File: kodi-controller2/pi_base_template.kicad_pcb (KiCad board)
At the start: 2 copper layers, 62 x 62.9 mm, 17 parts, among them P1 Raspberry_Pi_+_Conn, SW1 SW_PUSH_SMALL, SW2 SW_PUSH_SMALL, SW3 SW_PUSH_SMALL, SW4 SW_PUSH_SMALL

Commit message: Finished new board layout
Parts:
- moved R2 2.54 mm to (145.1, 114.4)
- turned P1 to 180 degrees
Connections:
- P1 pad 10: (no net) -> Net-(P1-Pad19)
- P1 pad 11: Net-(P1-Pad11) -> Net-(P1-Pad21)
- P1 pad 12: (no net) -> Net-(P1-Pad23)
- P1 pad 13: Net-(P1-Pad13) -> GND
- P1 pad 15: Net-(P1-Pad15) -> Net-(P1-Pad29)
- P1 pad 16: (no net) -> Net-(P1-Pad31)
- P1 pad 19: Net-(P1-Pad19) -> (no net)
- P1 pad 2: (no net) -> Net-(P1-Pad3)
- P1 pad 20: (no net) -> GND
- P1 pad 3: Net-(P1-Pad3) -> (no net)
- P1 pad 4: (no net) -> Net-(P1-Pad7)
- P1 pad 5: Net-(P1-Pad5) -> GND
- P1 pad 6: (no net) -> Net-(P1-Pad11)
- P1 pad 7: Net-(P1-Pad7) -> Net-(P1-Pad13)
- P1 pad 8: (no net) -> Net-(P1-Pad15)
- P1 pad 9: GND -> +3V3
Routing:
- net GND: track 0.00 -> 143.2 mm
- net +3V3: track 0.00 -> 127.2 mm, vias 0 -> 5
- net Net-(P1-Pad11): track 0.00 -> 73.4 mm
- net Net-(P1-Pad3): track 0.00 -> 69.1 mm
- net Net-(P1-Pad7): track 0.00 -> 68.5 mm
- net Net-(P1-Pad13): track 0.00 -> 58.6 mm
- net Net-(P1-Pad15): track 0.00 -> 45.2 mm
- net Net-(P1-Pad19): track 0.00 -> 43.1 mm
- net Net-(P1-Pad21): track 0.00 -> 33.6 mm
- net Net-(P1-Pad31): track 0.00 -> 29.0 mm
- net Net-(P1-Pad23): track 0.00 -> 27.3 mm
- net Net-(P1-Pad29): track 0.00 -> 25.2 mm
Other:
- board size 62 x 62.9 mm -> 109.2 x 62.9 mm

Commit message: KodeController2: Switched footprint pin positions for push switches.
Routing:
- net GND: track 143.2 -> 147.3 mm
- net Net-(P1-Pad19): track 43.1 -> 41.4 mm
- net Net-(P1-Pad15): track 45.2 -> 46.5 mm
- net Net-(P1-Pad13): track 58.6 -> 59.9 mm
- net Net-(P1-Pad21): track 33.6 -> 34.9 mm

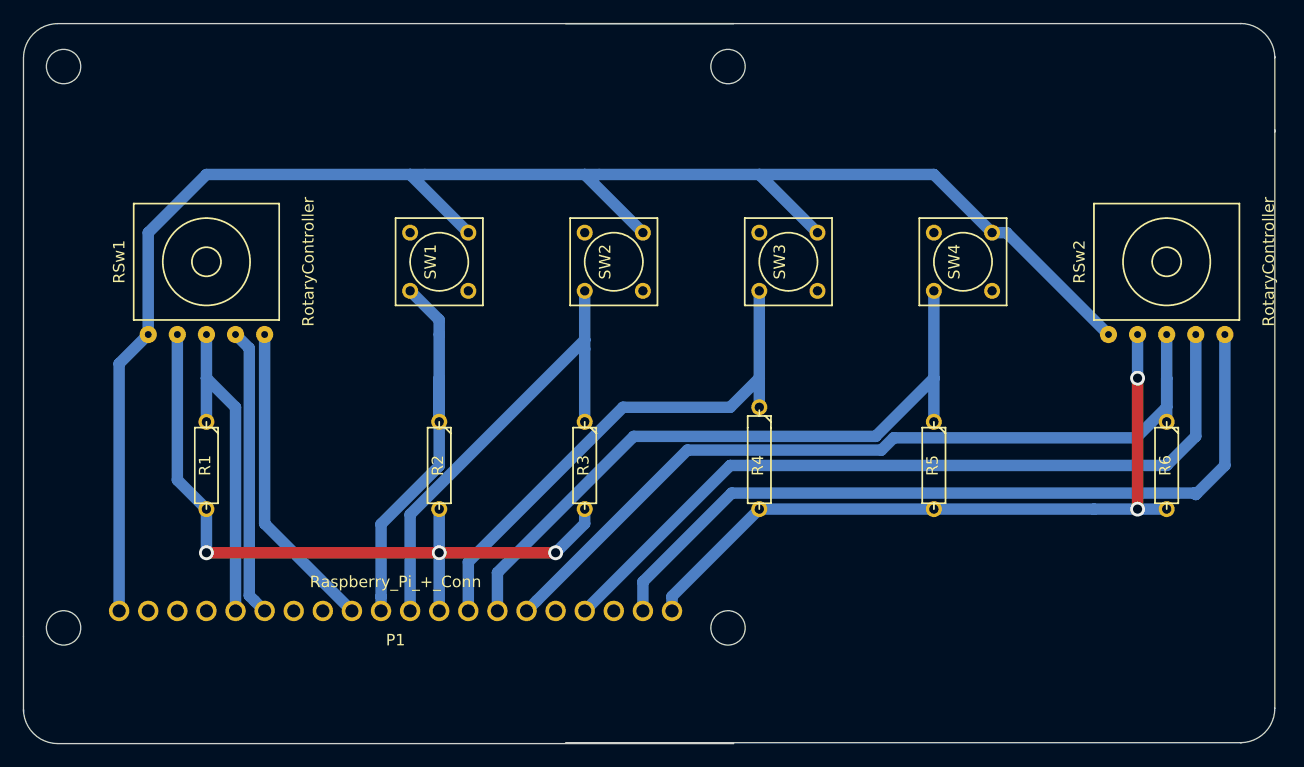
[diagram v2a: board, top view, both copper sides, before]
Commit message: Updated clearances.
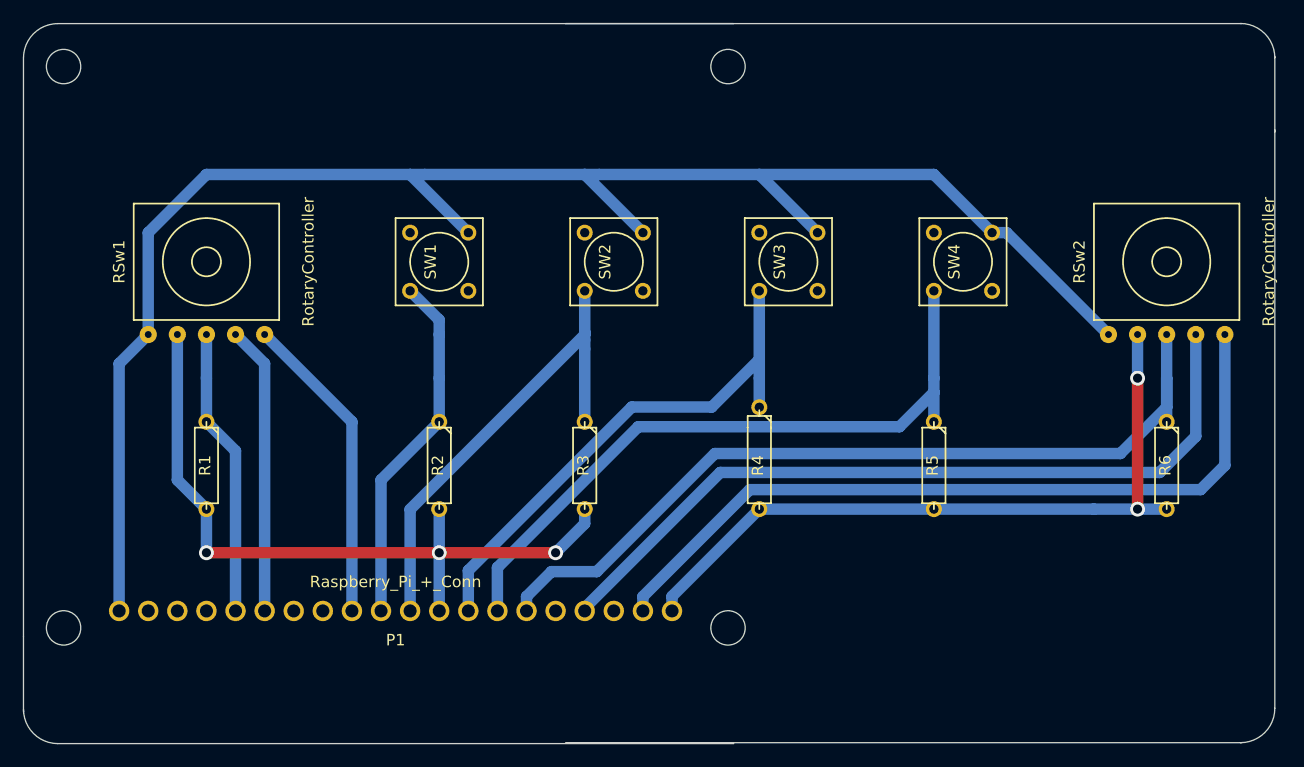
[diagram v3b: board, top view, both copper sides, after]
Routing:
- net Net-(P1-Pad31): track 29.0 -> 25.2 mm
- net Net-(P1-Pad21): track 34.9 -> 31.1 mm
- net Net-(P1-Pad3): track 69.1 -> 68.2 mm
- net Net-(P1-Pad11): track 73.4 -> 74.1 mm
- net Net-(P1-Pad19): track 41.4 -> 42.1 mm
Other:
- net class Default: clearance 0.2 -> 0.5
- rule trace_clearance: 0.2 -> 0.5
- rule trace_min: 0.1 -> 1
- rule via_min_size: 0.26 -> 1.3
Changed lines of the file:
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@@
     (user_trace_width 0.8)
     (user_trace_width 1)
-    (trace_clearance 0.2)
+    (trace_clearance 0.5)
     (zone_clearance 0.23)
     (zone_45_only no)
-    (trace_min 0.1)
+    (trace_min 1)
     (segment_width 0.2)
     (edge_width 0.1)
     (via_size 1.3)
     (via_drill 0.8)
-    (via_min_size 0.26)
+    (via_min_size 1.3)
     (via_min_drill 0.16)
     (user_via 0.4 0.22)
@@
   (net 13 "Net-(P1-Pad23)")
   (net_class Default "This is the default net class."
-    (clearance 0.2)
+    (clearance 0.5)
     (trace_width 1)
     (via_dia 1.3)
@@
   (segment (start 173 118.21) (end 188.24 118.21) (width 1) (layer B.Cu) (net 2))
   (segment (start 165.38 125.83) (end 173 118.21) (width 1) (layer B.Cu) (net 2))
-  (segment (start 162.84 124.56) (end 162.84 127.1) (width 1) (layer B.Cu) (net 3))
-  (segment (start 170.588501 116.811499) (end 162.84 124.56) (width 1) (layer B.Cu) (net 3))
-  (segment (start 211.1 116.94) (end 210.971499 116.811499) (width 1) (layer B.Cu) (net 3))
-  (segment (start 210.971499 116.811499) (end 170.588501 116.811499) (width 1) (layer B.Cu) (net 3))
-  (segment (start 213.64 114.4) (end 211.1 116.94) (width 1) (layer B.Cu) (net 3))
-  (segment (start 213.64 102.97) (end 213.64 114.4) (width 1) (layer B.Cu) (net 3))
-  (segment (start 170.46 114.4) (end 157.76 127.1) (width 1) (layer B.Cu) (net 4))
-  (segment (start 208.56 114.4) (end 170.46 114.4) (width 1) (layer B.Cu) (net 4))
-  (segment (start 211.1 111.86) (end 208.56 114.4) (width 1) (layer B.Cu) (net 4))
-  (segment (start 211.1 102.97) (end 211.1 111.86) (width 1) (layer B.Cu) (net 4))
-  (segment (start 153.568999 126.211001) (end 152.68 127.1) (width 1) (layer B.Cu) (net 5))
-  (segment (start 166.719989 113.060011) (end 153.568999 126.211001) (width 1) (layer B.Cu) (net 5))
-  (segment (start 205.891499 111.988501) (end 184.72857 111.988501) (width 1) (layer B.Cu) (net 5))
-  (segment (start 183.65706 113.060011) (end 166.719989 113.060011) (width 1) (layer B.Cu) (net 5))
-  (segment (start 208.56 109.32) (end 205.891499 111.988501) (width 1) (layer B.Cu) (net 5))
-  (segment (start 208.56 106.78) (end 208.56 109.32) (width 1) (layer B.Cu) (net 5))
-  (segment (start 184.72857 111.988501) (end 183.65706 113.060011) (width 1) (layer B.Cu) (net 5))
+  (segment (start 162.84 127.1) (end 162.84 125.842765) (width 1) (layer B.Cu) (net 3))
+  (segment (start 162.84 125.842765) (end 172.171266 116.511499) (width 1) (layer B.Cu) (net 3))
+  (segment (start 172.171266 116.511499) (end 211.528501 116.511499) (width 1) (layer B.Cu) (net 3))
+  (segment (start 211.528501 116.511499) (end 213.64 114.4) (width 1) (layer B.Cu) (net 3))
+  (segment (start 213.64 114.4) (end 213.64 102.97) (width 1) (layer B.Cu) (net 3))
+  (segment (start 157.76 127.1) (end 157.76 126.844278) (width 1) (layer B.Cu) (net 4))
+  (segment (start 157.76 126.844278) (end 169.592789 115.011489) (width 1) (layer B.Cu) (net 4))
+  (segment (start 169.592789 115.011489) (end 207.948511 115.011489) (width 1) (layer B.Cu) (net 4))
+  (segment (start 207.948511 115.011489) (end 211.1 111.86) (width 1) (layer B.Cu) (net 4))
+  (segment (start 211.1 111.86) (end 211.1 102.97) (width 1) (layer B.Cu) (net 4))
+  (segment (start 152.68 127.1) (end 152.68 125.842765) (width 1) (layer B.Cu) (net 5))
+  (segment (start 169.122934 113.36001) (end 204.51999 113.36001) (width 1) (layer B.Cu) (net 5))
+  (segment (start 152.68 125.842765) (end 154.852764 123.670001) (width 1) (layer B.Cu) (net 5))
+  (segment (start 158.812943 123.670001) (end 169.122934 113.36001) (width 1) (layer B.Cu) (net 5))
+  (segment (start 154.852764 123.670001) (end 158.812943 123.670001) (width 1) (layer B.Cu) (net 5))
+  (segment (start 204.51999 113.36001) (end 208.56 109.32) (width 1) (layer B.Cu) (net 5))
+  (segment (start 208.56 109.32) (end 208.56 106.78) (width 1) (layer B.Cu) (net 5))
   (segment (start 208.56 106.78) (end 208.56 110.59) (width 1) (layer B.Cu) (net 5))
   (segment (start 208.56 102.97) (end 208.56 106.78) (width 1) (layer B.Cu) (net 5))
+  (segment (start 188.24 106.78) (end 188.24 108.02) (width 1) (layer B.Cu) (net 6))
+  (segment (start 188.24 108.02) (end 188.24 110.59) (width 1) (layer B.Cu) (net 6))
+  (segment (start 150.14 127.1) (end 150.14 123.316218) (width 1) (layer B.Cu) (net 6))
+  (segment (start 150.14 123.316218) (end 162.437717 111.018501) (width 1) (layer B.Cu) (net 6))
+  (segment (start 162.437717 111.018501) (end 185.241499 111.018501) (width 1) (layer B.Cu) (net 6))
+  (segment (start 185.241499 111.018501) (end 188.24 108.02) (width 1) (layer B.Cu) (net 6))
   (segment (start 188.24 99.16) (end 188.24 106.78) (width 1) (layer B.Cu) (net 6))
-  (segment (start 188.24 106.78) (end 188.24 110.59) (width 1) (layer B.Cu) (net 6))
-  (segment (start 162.040218 111.86) (end 183.16 111.86) (width 1) (layer B.Cu) (net 6))
-  (segment (start 183.16 111.86) (end 188.24 106.78) (width 1) (layer B.Cu) (net 6))
-  (segment (start 150.14 127.1) (end 150.14 123.760218) (width 1) (layer B.Cu) (net 6))
-  (segment (start 150.14 123.760218) (end 162.040218 111.86) (width 1) (layer B.Cu) (net 6))
-  (segment (start 173 99.16) (end 173 106.78) (width 1) (layer B.Cu) (net 7))
-  (segment (start 147.6 122.819782) (end 161.099782 109.32) (width 1) (layer B.Cu) (net 7))
+  (segment (start 173 99.16) (end 173 105.15) (width 1) (layer B.Cu) (net 7))
+  (segment (start 173 105.15) (end 173 106.78) (width 1) (layer B.Cu) (net 7))
+  (segment (start 161.872172 109.3) (end 168.85 109.3) (width 1) (layer B.Cu) (net 7))
+  (segment (start 168.85 109.3) (end 173 105.15) (width 1) (layer B.Cu) (net 7))
+  (segment (start 147.6 127.1) (end 147.6 123.572172) (width 1) (layer B.Cu) (net 7))
+  (segment (start 147.6 123.572172) (end 161.872172 109.3) (width 1) (layer B.Cu) (net 7))
   (segment (start 173 106.78) (end 173 109.32) (width 1) (layer B.Cu) (net 7))
-  (segment (start 147.6 127.1) (end 147.6 122.819782) (width 1) (layer B.Cu) (net 7))
-  (segment (start 161.099782 109.32) (end 170.46 109.32) (width 1) (layer B.Cu) (net 7))
-  (segment (start 170.46 109.32) (end 173 106.78) (width 1) (layer B.Cu) (net 7))
+  (segment (start 157.76 99.16) (end 157.76 102.74) (width 1) (layer B.Cu) (net 9))
+  (segment (start 157.76 102.74) (end 157.76 103.440218) (width 1) (layer B.Cu) (net 9))
+  (segment (start 142.52 127.1) (end 142.52 118.236218) (width 1) (layer B.Cu) (net 9))
+  (segment (start 142.52 118.236218) (end 157.76 102.996218) (width 1) (layer B.Cu) (net 9))
+  (segment (start 157.76 102.996218) (end 157.76 102.74) (width 1) (layer B.Cu) (net 9))
   (segment (start 157.76 110.59) (end 157.76 104.24) (width 1) (layer B.Cu) (net 9))
   (segment (start 157.76 104.24) (end 157.76 103.440218) (width 1) (layer B.Cu) (net 9))
-  (segment (start 157.76 99.16) (end 157.76 103.440218) (width 1) (layer B.Cu) (net 9))
-  (segment (start 142.52 127.1) (end 142.52 118.680218) (width 1) (layer B.Cu) (net 9))
-  (segment (start 142.52 118.680218) (end 157.76 103.440218) (width 1) (layer B.Cu) (net 9))
-  (segment (start 127.28 109.32) (end 127.28 127.1) (width 1) (layer B.Cu) (net 10))
+  (segment (start 124.74 110.59) (end 127.28 113.13) (width 1) (layer B.Cu) (net 10))
+  (segment (start 127.28 113.13) (end 127.28 127.1) (width 1) (layer B.Cu) (net 10))
   (segment (start 124.74 106.78) (end 124.74 110.59) (width 1) (layer B.Cu) (net 10))
   (segment (start 124.74 102.97) (end 124.74 106.78) (width 1) (layer B.Cu) (net 10))
-  (segment (start 124.74 106.78) (end 127.28 109.32) (width 1) (layer B.Cu) (net 10))
+  (segment (start 139.98 127.1) (end 139.98 115.67) (width 1) (layer B.Cu) (net 11))
+  (segment (start 139.98 115.67) (end 145.06 110.59) (width 1) (layer B.Cu) (net 11))
   (segment (start 145.06 101.7) (end 145.06 102.97) (width 1) (layer B.Cu) (net 11))
   (segment (start 142.52 99.16) (end 145.06 101.7) (width 1) (layer B.Cu) (net 11))
   (segment (start 145.06 106.78) (end 145.06 102.97) (width 1) (layer B.Cu) (net 11))
-  (segment (start 145.06 114.443147) (end 139.98 119.523147) (width 1) (layer B.Cu) (net 11))
   (segment (start 145.06 110.59) (end 145.06 106.78) (width 1) (layer B.Cu) (net 11))
-  (segment (start 139.98 125.842765) (end 139.98 127.1) (width 1) (layer B.Cu) (net 11))
-  (segment (start 145.06 106.78) (end 145.06 114.443147) (width 1) (layer B.Cu) (net 11))
-  (segment (start 139.98 119.523147) (end 139.98 125.842765) (width 1) (layer B.Cu) (net 11))
-  (segment (start 128.931001 126.211001) (end 129.82 127.1) (width 1) (layer B.Cu) (net 12))
-  (segment (start 128.480011 125.760011) (end 128.931001 126.211001) (width 1) (layer B.Cu) (net 12))
-  (segment (start 128.480011 104.170011) (end 128.480011 125.760011) (width 1) (layer B.Cu) (net 12))
-  (segment (start 127.28 102.97) (end 128.480011 104.170011) (width 1) (layer B.Cu) (net 12))
-  (segment (start 129.82 102.97) (end 129.82 119.48) (width 1) (layer B.Cu) (net 13))
-  (segment (start 129.82 119.48) (end 137.44 127.1) (width 1) (layer B.Cu) (net 13))
+  (segment (start 127.28 102.97) (end 129.82 105.51) (width 1) (layer B.Cu) (net 12))
+  (segment (start 129.82 105.51) (end 129.82 127.1) (width 1) (layer B.Cu) (net 12))
+  (segment (start 129.82 102.97) (end 137.44 110.59) (width 1) (layer B.Cu) (net 13))
+  (segment (start 137.44 110.59) (end 137.44 127.1) (width 1) (layer B.Cu) (net 13))
 )

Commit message: Filled the board once more.
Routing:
- net (no net): track 0.00 -> 186.0 mm
- added copper zone on B.Cu, net (none)
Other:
- board text added: "by KingWarin.de"
